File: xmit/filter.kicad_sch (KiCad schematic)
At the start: 31 parts, among them U1 74LVC1G66, U2 74LVC1G66, U3 74LVC1G66, U4 74LVC1G66, U5 74LVC1G66, U6 74LVC1G66

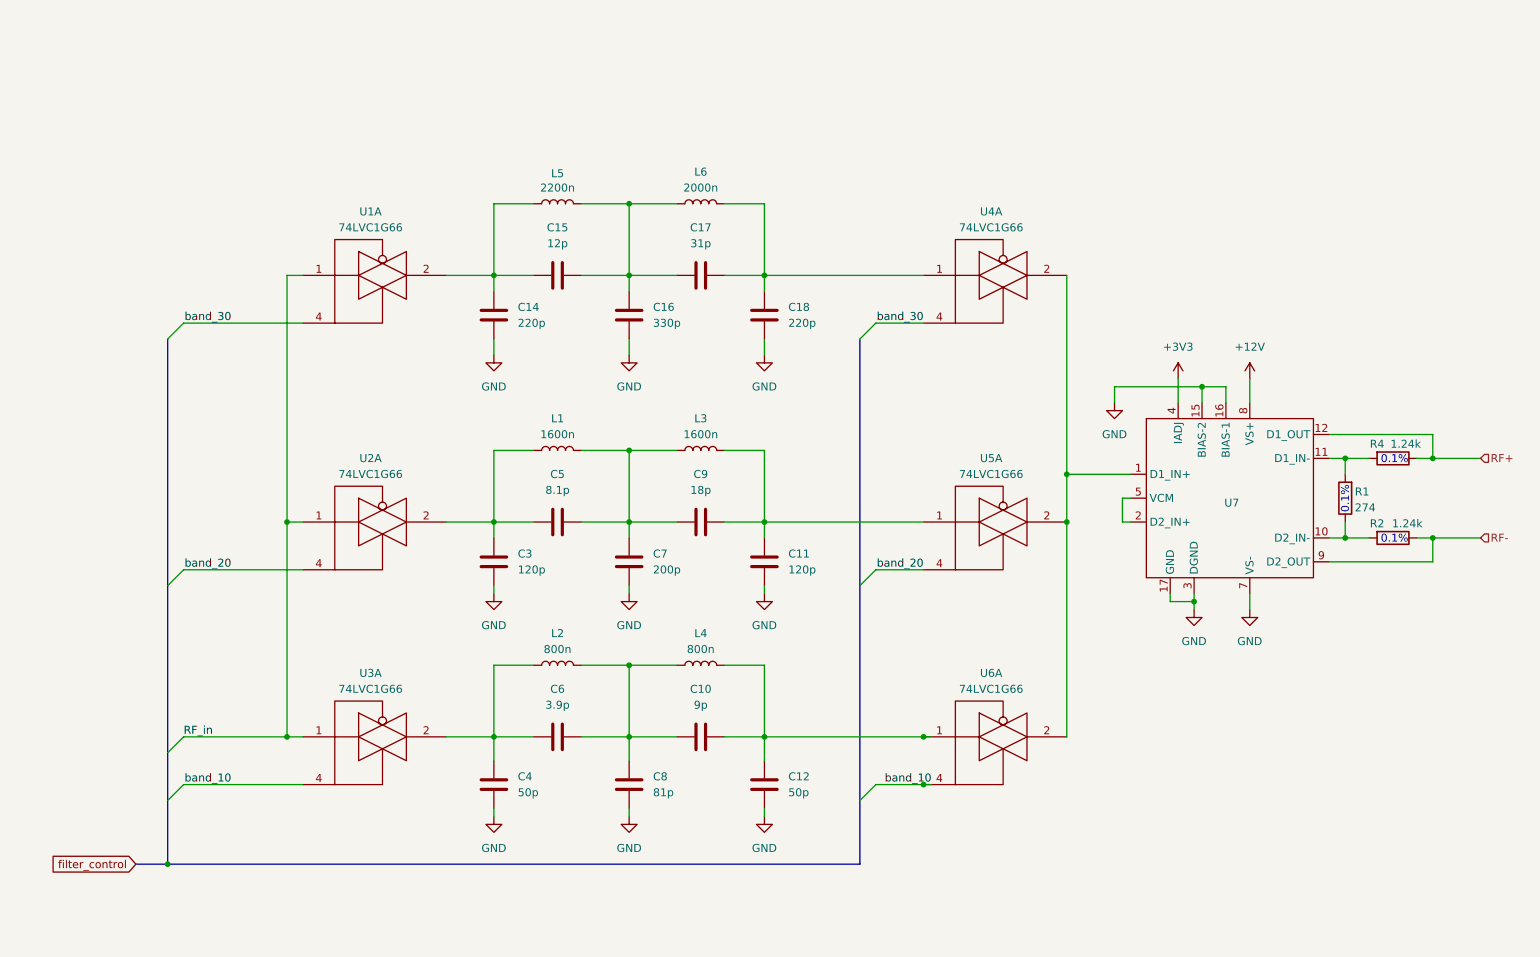
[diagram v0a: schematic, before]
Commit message: WIP commit, but the circuit is nearly done and PCB is beginning for form.
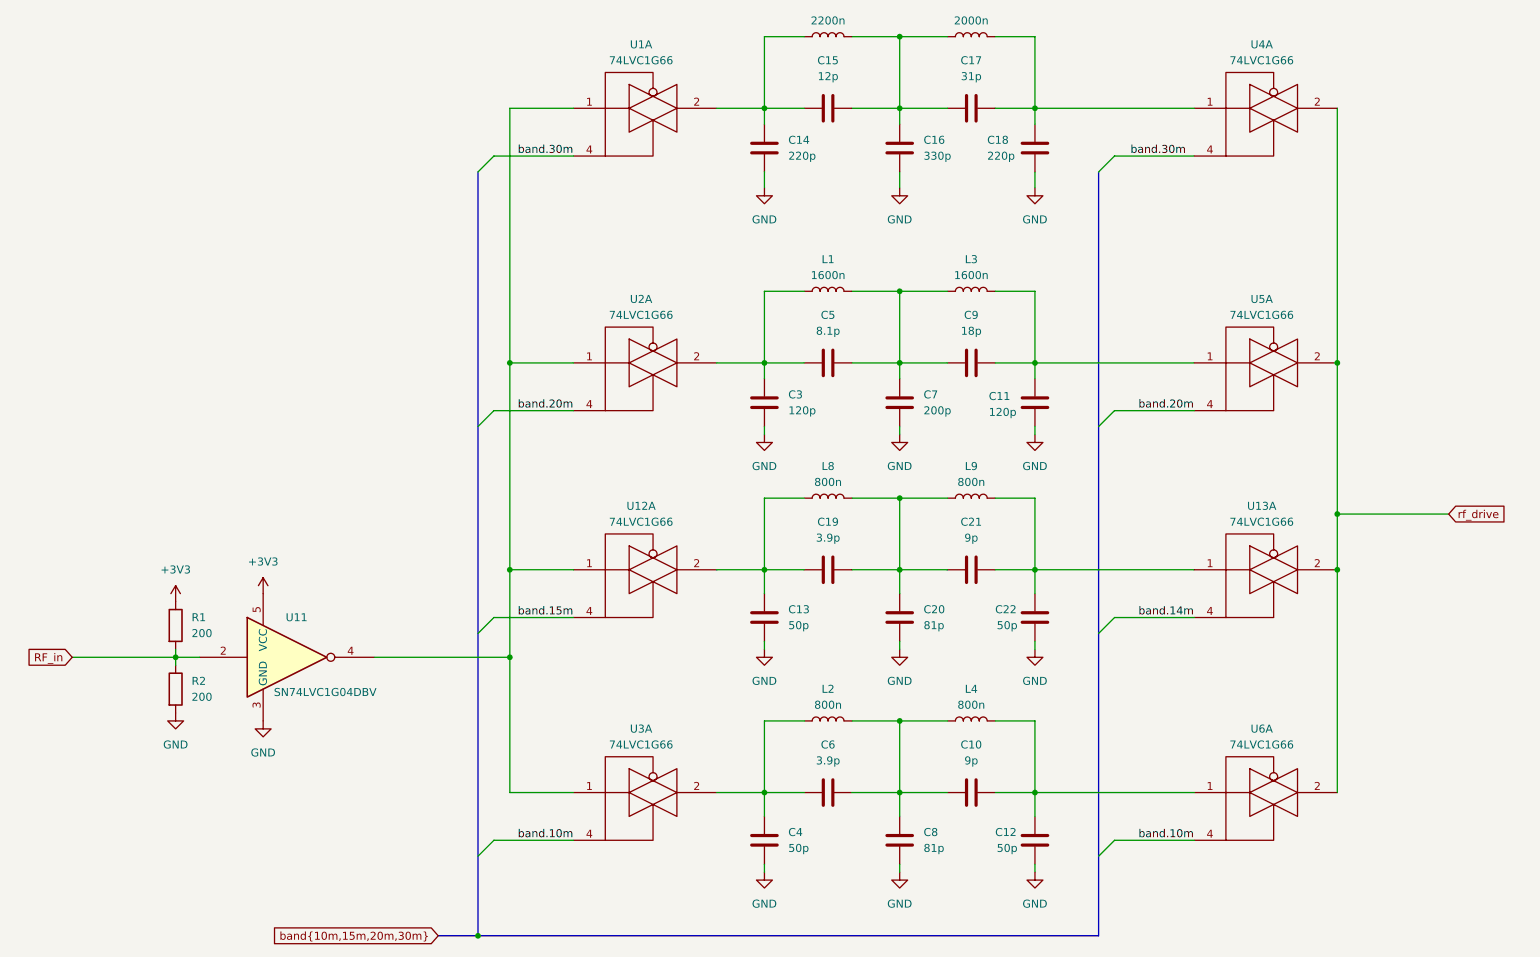
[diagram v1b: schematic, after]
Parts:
- removed R4: 1.24k, Resistor_SMD:R_0603_1608Metric_Pad0.98x0.95mm_HandSolder, symbol Device:R
- removed U7: (no value), Package_DFN_QFN:VQFN-16-1EP_3x3mm_P0.5mm_EP1.8x1.8mm_ThermalVias, symbol Amplifier_Difference:THS6222RGT
- added C13, C22: 50p, Capacitor_SMD:C_0805_2012Metric_Pad1.18x1.45mm_HandSolder, symbol Device:C
- added C19: 3.9p, Capacitor_SMD:C_0805_2012Metric_Pad1.18x1.45mm_HandSolder, symbol Device:C
- added C20: 81p, Capacitor_SMD:C_0805_2012Metric_Pad1.18x1.45mm_HandSolder, symbol Device:C
- added C21: 9p, Capacitor_SMD:C_0805_2012Metric_Pad1.18x1.45mm_HandSolder, symbol Device:C
- added L8, L9: 800n, Inductor_SMD:L_0805_2012Metric_Pad1.05x1.20mm_HandSolder, symbol Device:L
- added U11: SN74LVC1G04DBV, Package_TO_SOT_SMD:SOT-23-5_HandSoldering, symbol 74xGxx:74LVC1G04
- added U12, U13: 74LVC1G66, Package_TO_SOT_SMD:SOT-23-5_HandSoldering, symbol 74xGxx:74LVC1G66
- R1: value 274 -> 200; footprint Resistor_SMD:R_0603_1608Metric_Pad0.98x0.95mm_HandSolder -> Capacitor_SMD:C_0402_1005Metric
- R2: value 1.24k -> 200; footprint Resistor_SMD:R_0603_1608Metric_Pad0.98x0.95mm_HandSolder -> Capacitor_SMD:C_0402_1005Metric
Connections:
- net RF- is gone; now on net RF_in: R2.1
- net +3V3: now also R1.1, U11.5 (VCC)
- net GND: now also R2.2, C13.2, C20.2, C22.2, U11.3 (GND)
- net RF_in: now also R1.2, U11.2; no longer U1.1, U2.1, U3.1
- net rf_drive: now reaches U4.2, U5.2, U6.2
- net rf_drive: now also U13.2
- net band_10 renamed band.10m
- net band_20 renamed band.20m
- net band_30 renamed band.30m
- new net: C13.1, C19.1, L8.1, U12.2
- new net: C19.2, C20.1, C21.1, L8.2, L9.1
- new net: U1.1, U11.4, U12.1, U2.1, U3.1
- new net: C21.2, C22.1, L9.2, U13.1
- new net band.14m: U13.4
- new net band.15m: U12.4
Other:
- note removed: "0.1%"
- moved on the sheet: C10, C11, C12, C14, C15, C16, C17, C18, C3, C4, C5, C6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

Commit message: Updated filters and improved amp
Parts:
- C10: value 9p -> 5.6p
- C12, C4: value 50p -> 33p
- C6: value 3.9p -> 2.2p
- C8: value 81p -> 72p
- L2, L4: value 800n -> 56n
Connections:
- net band.14m is gone; now on net band.10m: U13.4
- net band.15m is gone; now on net band.10m: U12.4
- net band.10m: no longer U3.4, U6.4
- new net band.2m: U3.4, U6.4
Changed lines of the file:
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@@
 		)
 	)
-	(label "band.15m"
+	(label "band.10m"
 		(at 106.68 111.76 0)
 		(effects
@@
 		)
 	)
-	(label "band.10m"
+	(label "band.2m"
 		(at 106.68 147.32 0)
 		(effects
@@
 		)
 	)
-	(label "band.14m"
+	(label "band.10m"
 		(at 205.74 111.76 0)
 		(effects
@@
 		)
 	)
-	(label "band.10m"
+	(label "band.2m"
 		(at 205.74 147.32 0)
 		(effects
@@
 		)
 	)
-	(global_label "band{10m,15m,20m,30m}"
+	(global_label "band{2m,10m,20m,30m}"
 		(shape input)
 		(at 93.98 162.56 180)
@@
 		)
 		(property "Intersheetrefs" "${INTERSHEET_REFS}"
-			(at 66.4418 162.56 0)
+			(at 67.6513 162.56 0)
 			(show_name no)
 			(do_not_autoplace no)
@@
 			)
 		)
-		(property "Value" "800n"
+		(property "Value" "56n"
 			(at 179.07 125.73 90)
 			(show_name no)
@@
 			)
 		)
-		(property "Value" "81p"
+		(property "Value" "72p"
 			(at 171.45 148.5899 0)
 			(show_name no)
@@
 			)
 		)
-		(property "Value" "9p"
+		(property "Value" "5.6p"
 			(at 179.07 134.62 90)
 			(show_name no)
@@
 			)
 		)
-		(property "Value" "50p"
+		(property "Value" "33p"
 			(at 183.134 148.59 0)
 			(show_name no)
@@
 			)
 		)
-		(property "Value" "800n"
+		(property "Value" "56n"
 			(at 156.21 125.73 90)
 			(show_name no)
@@
 			)
 		)
-		(property "Datasheet" ""
+		(property "Datasheet" "https://pim.murata.com/asset/pim4/inductor/JELF243A-0084_PDF_INDUCTOR"
 			(at 156.21 128.27 0)
 			(hide yes)
@@
 			)
 		)
-		(property "Description" "Inductor"
+		(property "Description" "56nH 0805 SMD Murata part LQW2BAS56NJ00L"
 			(at 156.21 128.27 0)
 			(hide yes)
@@
 			)
 		)
-		(property "Value" "50p"
+		(property "Value" "33p"
 			(at 149.86 148.5899 0)
 			(show_name no)
@@
 			)
 		)
-		(property "Value" "3.9p"
+		(property "Value" "2.2p"
 			(at 156.21 134.62 90)
 			(show_name no)

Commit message: Another WIP on transmitter layout. Should be pretty close.
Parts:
- L1, L3, L5, L6: footprint Inductor_SMD:L_1206_3216Metric_Pad1.22x1.90mm_HandSolder -> Inductor_SMD:L_0805_2012Metric_Pad1.05x1.20mm_HandSolder
- R1, R2: footprint Capacitor_SMD:C_0402_1005Metric -> Resistor_SMD:R_0805_2012Metric_Pad1.20x1.40mm_HandSolder
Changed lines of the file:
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@@
 			)
 		)
-		(property "Footprint" "Inductor_SMD:L_1206_3216Metric_Pad1.22x1.90mm_HandSolder"
+		(property "Footprint" "Inductor_SMD:L_0805_2012Metric_Pad1.05x1.20mm_HandSolder"
 			(at 156.21 19.05 0)
 			(hide yes)
@@
 			)
 		)
-		(property "Footprint" "Inductor_SMD:L_1206_3216Metric_Pad1.22x1.90mm_HandSolder"
+		(property "Footprint" "Inductor_SMD:L_0805_2012Metric_Pad1.05x1.20mm_HandSolder"
 			(at 156.21 59.69 0)
 			(hide yes)
@@
 			)
 		)
-		(property "Footprint" "Inductor_SMD:L_1206_3216Metric_Pad1.22x1.90mm_HandSolder"
+		(property "Footprint" "Inductor_SMD:L_0805_2012Metric_Pad1.05x1.20mm_HandSolder"
 			(at 179.07 19.05 0)
 			(hide yes)
@@
 			)
 		)
-		(property "Footprint" "Inductor_SMD:L_1206_3216Metric_Pad1.22x1.90mm_HandSolder"
+		(property "Footprint" "Inductor_SMD:L_0805_2012Metric_Pad1.05x1.20mm_HandSolder"
 			(at 179.07 59.69 0)
 			(hide yes)
@@
 			)
 		)
-		(property "Footprint" "Capacitor_SMD:C_0402_1005Metric"
+		(property "Footprint" "Resistor_SMD:R_0805_2012Metric_Pad1.20x1.40mm_HandSolder"
 			(at 50.292 123.19 90)
 			(hide yes)
@@
 			)
 		)
-		(property "Footprint" "Capacitor_SMD:C_0402_1005Metric"
+		(property "Footprint" "Resistor_SMD:R_0805_2012Metric_Pad1.20x1.40mm_HandSolder"
 			(at 50.292 113.03 90)
 			(hide yes)
